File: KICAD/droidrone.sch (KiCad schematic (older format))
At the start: 48 parts, among them U4 LP2950L-3.3V, Y1 Crystal

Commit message: kicad add usb
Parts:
- removed 10k5, 10k6: 10k, lib:R-tate, symbol R
- added P?: USB_A, symbol USB_A
- U?: symbol 7805 -> 7805-RESCUE-droidrone
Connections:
- wire segments 106 -> 103
- no-connect marks 28 -> 32
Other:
- moved on the sheet: 1k1, 1k2, LED1, LED2
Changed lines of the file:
@@
 EESchema Schematic File Version 2
+LIBS:droidrone-rescue
 LIBS:power
 LIBS:device
@@
 U 1 1 580D711D
 P 4700 6700
-F 0 "RN42XV1" H 4700 7150 60  0000 C CNN
+F 0 "RN42XV1" H 4700 7050 60  0000 C CNN
 F 1 "RN42XV" H 4700 7050 60  0001 C CNN
 F 2 "lib:RN42XV" H 4700 6700 60  0001 C CNN
@@
 U 1 1 580E898B
 P 3300 6650
-F 0 "RN4020" H 3300 7250 60  0000 C CNN
+F 0 "RN4020" H 3300 7150 60  0000 C CNN
 F 1 "RN4020" H 3300 7150 60  0001 C CNN
 F 2 "lib:RN2040" H 3300 6650 60  0001 C CNN
@@
 L R 1k1
 U 1 1 580EB00D
-P 2000 6400
-F 0 "1k1" V 2080 6400 50  0000 C CNN
-F 1 "1k" V 2000 6400 50  0001 C CNN
-F 2 "lib:R-tate" V 1930 6400 50  0001 C CNN
-F 3 "" H 2000 6400 50  0000 C CNN
-	1    2000 6400
-	0    1    1    0
-$EndComp
-$Comp
-L R 1k2
-U 1 1 580EB146
-P 2000 6600
-F 0 "1k2" V 2080 6600 50  0000 C CNN
-F 1 "1k" V 2000 6600 50  0001 C CNN
-F 2 "lib:R-tate" V 1930 6600 50  0001 C CNN
-F 3 "" H 2000 6600 50  0000 C CNN
-	1    2000 6600
+P 2300 6400
+F 0 "1k1" V 2380 6400 50  0000 C CNN
+F 1 "1k" V 2300 6400 50  0001 C CNN
+F 2 "lib:R-tate" V 2230 6400 50  0001 C CNN
+F 3 "" H 2300 6400 50  0000 C CNN
+	1    2300 6400
 	0    1    1    0
 $EndComp
@@
 L LED LED1
 U 1 1 580EC3D9
-P 1650 6400
-F 0 "LED1" H 1650 6500 50  0000 C CNN
-F 1 "LED" H 1450 6500 50  0000 C CNN
-F 2 "LEDs:LED-5MM" H 1650 6400 50  0001 C CNN
-F 3 "" H 1650 6400 50  0000 C CNN
-	1    1650 6400
+P 1950 6400
+F 0 "LED1" H 1950 6500 50  0000 C CNN
+F 1 "LED" H 1750 6500 50  0000 C CNN
+F 2 "LEDs:LED-5MM" H 1950 6400 50  0001 C CNN
+F 3 "" H 1950 6400 50  0000 C CNN
+	1    1950 6400
 	1    0    0    -1
 $EndComp
@@
 L LED LED2
 U 1 1 580EC4D0
-P 1650 6600
-F 0 "LED2" H 1650 6700 50  0000 C CNN
-F 1 "LED" H 1450 6700 50  0000 C CNN
-F 2 "LEDs:LED-5MM" H 1650 6600 50  0001 C CNN
-F 3 "" H 1650 6600 50  0000 C CNN
-	1    1650 6600
+P 1950 6600
+F 0 "LED2" H 1950 6700 50  0000 C CNN
+F 1 "LED" H 1750 6700 50  0000 C CNN
+F 2 "LEDs:LED-5MM" H 1950 6600 50  0001 C CNN
+F 3 "" H 1950 6600 50  0000 C CNN
+	1    1950 6600
 	1    0    0    -1
 $EndComp
@@
 L GND #PWR049
 U 1 1 580EC7D8
-P 1450 6400
-F 0 "#PWR049" H 1450 6150 50  0001 C CNN
-F 1 "GND" H 1450 6250 50  0000 C CNN
-F 2 "" H 1450 6400 50  0000 C CNN
-F 3 "" H 1450 6400 50  0000 C CNN
-	1    1450 6400
+P 1750 6400
+F 0 "#PWR049" H 1750 6150 50  0001 C CNN
+F 1 "GND" H 1750 6250 50  0000 C CNN
+F 2 "" H 1750 6400 50  0000 C CNN
+F 3 "" H 1750 6400 50  0000 C CNN
+	1    1750 6400
 	0    1    1    0
 $EndComp
@@
 L GND #PWR050
 U 1 1 580EC8C5
-P 1450 6600
-F 0 "#PWR050" H 1450 6350 50  0001 C CNN
-F 1 "GND" H 1450 6450 50  0000 C CNN
-F 2 "" H 1450 6600 50  0000 C CNN
-F 3 "" H 1450 6600 50  0000 C CNN
-	1    1450 6600
+P 1750 6600
+F 0 "#PWR050" H 1750 6350 50  0001 C CNN
+F 1 "GND" H 1750 6450 50  0000 C CNN
+F 2 "" H 1750 6600 50  0000 C CNN
+F 3 "" H 1750 6600 50  0000 C CNN
+	1    1750 6600
 	0    1    1    0
 $EndComp
@@
 	3300 5900 3300 6000
 Connection ~ 1800 3600
-Wire Wire Line
-	10250 2250 10250 2200
 Connection ~ 3200 3600
-$Comp
-L R 10k6
-U 1 1 581115B0
-P 9150 6150
-F 0 "10k6" V 9230 6150 50  0000 C CNN
-F 1 "10k" V 9150 6150 50  0001 C CNN
-F 2 "lib:R-tate" V 9080 6150 50  0001 C CNN
-F 3 "" H 9150 6150 50  0000 C CNN
-	1    9150 6150
-	1    0    0    -1
-$EndComp
-$Comp
-L R 10k5
-U 1 1 581116D8
-P 9650 6200
-F 0 "10k5" V 9730 6200 50  0000 C CNN
-F 1 "10k" V 9650 6200 50  0001 C CNN
-F 2 "lib:R-tate" V 9580 6200 50  0001 C CNN
-F 3 "" H 9650 6200 50  0000 C CNN
-	1    9650 6200
-	1    0    0    -1
-$EndComp
 $Comp
 L +6V #PWR073
@@
 $EndComp
 Wire Wire Line
-	2150 6400 2450 6400
-Wire Wire Line
-	2150 6600 2450 6600
-Connection ~ 2200 6400
-Wire Wire Line
-	2450 6500 2250 6500
-Connection ~ 2300 6600
+	2450 6400 2450 6400
+Wire Wire Line
+	2450 6600 2450 6600
 $Comp
 L ATMEGA328P-A IC?
@@
 NoConn ~ 3400 7300
 NoConn ~ 3200 7300
-Wire Wire Line
-	2450 6900 2450 7000
 $Comp
 L GND #PWR?
@@
 $EndComp
 $Comp
-L 7805 U?
+L 7805-RESCUE-droidrone U?
 U 1 1 5888277B
 P 2200 3650
@@
 	1    0    0    -1
 $EndComp
+$Comp
+L R 1k2
+U 1 1 580EB146
+P 2300 6600
+F 0 "1k2" V 2380 6600 50  0000 C CNN
+F 1 "1k" V 2300 6600 50  0001 C CNN
+F 2 "lib:R-tate" V 2230 6600 50  0001 C CNN
+F 3 "" H 2300 6600 50  0000 C CNN
+	1    2300 6600
+	0    1    1    0
+$EndComp
+$Comp
+L +3.3V #PWR?
+U 1 1 58887043
+P 2450 6900
+F 0 "#PWR?" H 2450 6750 50  0001 C CNN
+F 1 "+3.3V" H 2450 7040 50  0000 C CNN
+F 2 "" H 2450 6900 50  0000 C CNN
+F 3 "" H 2450 6900 50  0000 C CNN
+	1    2450 6900
+	0    -1   -1   0
+$EndComp
+NoConn ~ 2450 6500
+$Comp
+L USB_A P?
+U 1 1 5889001F
+P 2700 2550
+F 0 "P?" H 2900 2350 50  0000 C CNN
+F 1 "USB_A" H 2650 2750 50  0000 C CNN
+F 2 "" V 2650 2450 50  0000 C CNN
+F 3 "" V 2650 2450 50  0000 C CNN
+	1    2700 2550
+	1    0    0    -1
+$EndComp
+NoConn ~ 2600 2850
+NoConn ~ 2700 2850
+$Comp
+L +5V #PWR?
+U 1 1 5889070E
+P 2500 2850
+F 0 "#PWR?" H 2500 2700 50  0001 C CNN
+F 1 "+5V" H 2500 2990 50  0000 C CNN
+F 2 "" H 2500 2850 50  0000 C CNN
+F 3 "" H 2500 2850 50  0000 C CNN
+	1    2500 2850
+	-1   0    0    1
+$EndComp
+$Comp
+L GND #PWR?
+U 1 1 58890B52
+P 2800 2850
+F 0 "#PWR?" H 2800 2600 50  0001 C CNN
+F 1 "GND" H 2800 2700 50  0000 C CNN
+F 2 "" H 2800 2850 50  0000 C CNN
+F 3 "" H 2800 2850 50  0000 C CNN
+	1    2800 2850
+	1    0    0    -1
+$EndComp
+NoConn ~ 3000 2450
 $EndSCHEMATC

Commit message: kicad chg1.
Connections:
- wire segments 103 -> 104
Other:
- moved on the sheet: P?
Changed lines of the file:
@@
 	6200 3800 6200 3900
 Wire Wire Line
-	6200 3900 6750 3900
-Wire Wire Line
-	6750 3900 6750 3550
+	6750 3900 6200 3900
+Wire Wire Line
+	6750 3600 6750 3900
 Connection ~ 6750 3700
 Wire Wire Line
 	6750 3450 6450 3450
 Wire Wire Line
-	6450 3350 6450 3700
+	6450 3300 6450 3700
 Connection ~ 6450 3700
 Wire Wire Line
-	7050 3450 7200 3450
-Wire Wire Line
-	7050 3450 7050 3700
+	7050 3400 7050 3700
 $Comp
 L GND #PWR?
@@
 L CONN_01X03 P?
 U 1 1 587C7767
-P 7400 3450
-F 0 "P?" H 7400 3650 50  0000 C CNN
-F 1 "CONN_01X03" V 7500 3450 50  0000 C CNN
-F 2 "" H 7400 3450 50  0000 C CNN
-F 3 "" H 7400 3450 50  0000 C CNN
-	1    7400 3450
-	1    0    0    -1
-$EndComp
-Wire Wire Line
-	6450 3350 7200 3350
+P 7400 3400
+F 0 "P?" H 7400 3600 50  0000 C CNN
+F 1 "CONN_01X03" V 7500 3400 50  0000 C CNN
+F 2 "" H 7400 3400 50  0000 C CNN
+F 3 "" H 7400 3400 50  0000 C CNN
+	1    7400 3400
+	1    0    0    -1
+$EndComp
+Wire Wire Line
+	6450 3300 7200 3300
 Connection ~ 6450 3450
 Connection ~ 7050 3450
 Wire Wire Line
-	6750 3550 7200 3550
+	6750 3600 7200 3600
 NoConn ~ 3500 7300
 NoConn ~ 3400 7300
@@
 $EndComp
 NoConn ~ 3000 2450
+Wire Wire Line
+	7200 3600 7200 3500
+Wire Wire Line
+	7050 3400 7200 3400
 $EndSCHEMATC

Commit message: kicad add usb
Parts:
- removed IC?: ATMEGA328P-A, TQFP32, symbol ATMEGA328P-A
- removed P?: CONN_01X03, symbol CONN_01X03
- added 0.1uF2: 0.1uF, Capacitors_ThroughHole:C_Rect_L4_W2.5_P2.5, symbol C
- added 10k4: 10k, lib:R-tate, symbol R
- added D17: CONN_01X03, Pin_Headers:Pin_Header_Straight_1x03, symbol CONN_01X03
- added IC1: ATMEGA328PB, lib:LQFP-32_7x7mm_Pitch0.8mm, symbol ATMEGA328PB
- added P4, P7: CONN_01X02, Pin_Headers:Pin_Header_Straight_1x02_Pitch2.54mm, symbol CONN_01X02
- added P5: CONN_01X04, Pin_Headers:Pin_Header_Straight_1x04_Pitch2.00mm, symbol CONN_01X04
- P2, P3: renamed from P?; footprint (none) -> Pin_Headers:Pin_Header_Straight_1x06_Pitch2.54mm
- P6: renamed from P?; footprint (none) -> Pin_Headers:Pin_Header_Straight_1x04_Pitch2.00mm
- Y1: footprint Crystals:Crystal_HC52-U_Vertical -> Crystals:Crystal_HC49-U-3pin_Vertical
- gave numbers to parts that had none: 2
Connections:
- wire segments 104 -> 120
- no-connect marks 32 -> 29
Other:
- moved on the sheet: 0.1uF5, 0.1uF6, 10k1, 10k2, 10k3, 1k4, 1k5, D10, D12, D13, D14, D15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

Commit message: foot print update
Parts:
- 0.1uF1, 0.1uF2, 0.1uF4, 0.1uF5, 0.1uF6, 22pF1, 22pF2: footprint Capacitors_ThroughHole:C_Rect_L4_W2.5_P2.5 -> Capacitors_ThroughHole:C_Rect_L4.0mm_W2.5mm_P2.50mm
- 100uF10V1, 47uF10V1: footprint Capacitors_ThroughHole:C_Radial_D5_L6_P2.5 -> Capacitors_ThroughHole:CP_Radial_D8.0mm_P2.50mm
- 10k1, 10k2, 10k3, 10k4, 1k1, 1k2, 1k3, 1k4, 1k5, 2.2k1, 3.3k1: footprint lib:R-tate -> Resistors_ThroughHole:R_Axial_DIN0204_L3.6mm_D1.6mm_P2.54mm_Vertical
- D10, D12, D13, D14, D15, D16, D17, D2, D4, D7, D8, D9: footprint Pin_Headers:Pin_Header_Straight_1x03 -> Pin_Headers:Pin_Header_Straight_1x03_Pitch2.54mm
- LED1, LED2, LED3, LED4: footprint LEDs:LED-5MM -> LEDs:LED_D5.0mm
- No-BEC1: footprint Pin_Headers:Pin_Header_Straight_1x02 -> Pin_Headers:Pin_Header_Straight_1x02_Pitch2.54mm
- P1: footprint (none) -> Connect:USB_A
- P6: footprint Pin_Headers:Pin_Header_Straight_1x04_Pitch2.00mm -> Pin_Headers:Pin_Header_Straight_1x06_Pitch2.54mm
- U1: footprint (none) -> TO_SOT_Packages_THT:TO-220_Neutral123_Vertical_LargePads

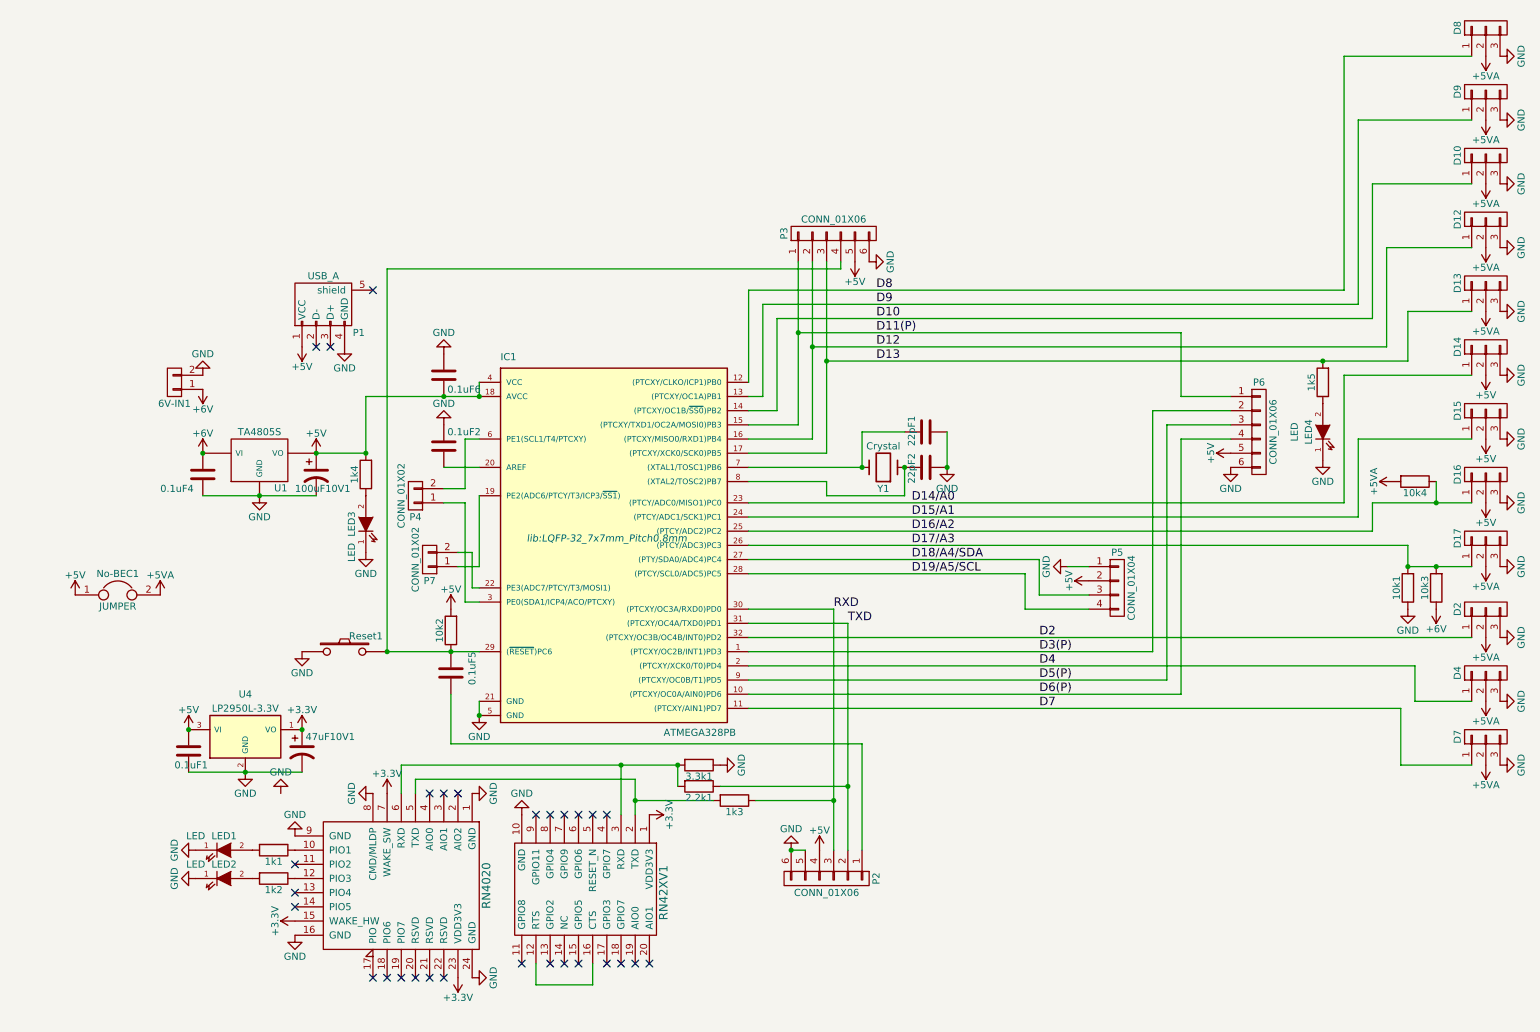
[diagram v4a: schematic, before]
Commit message: add sub pcb
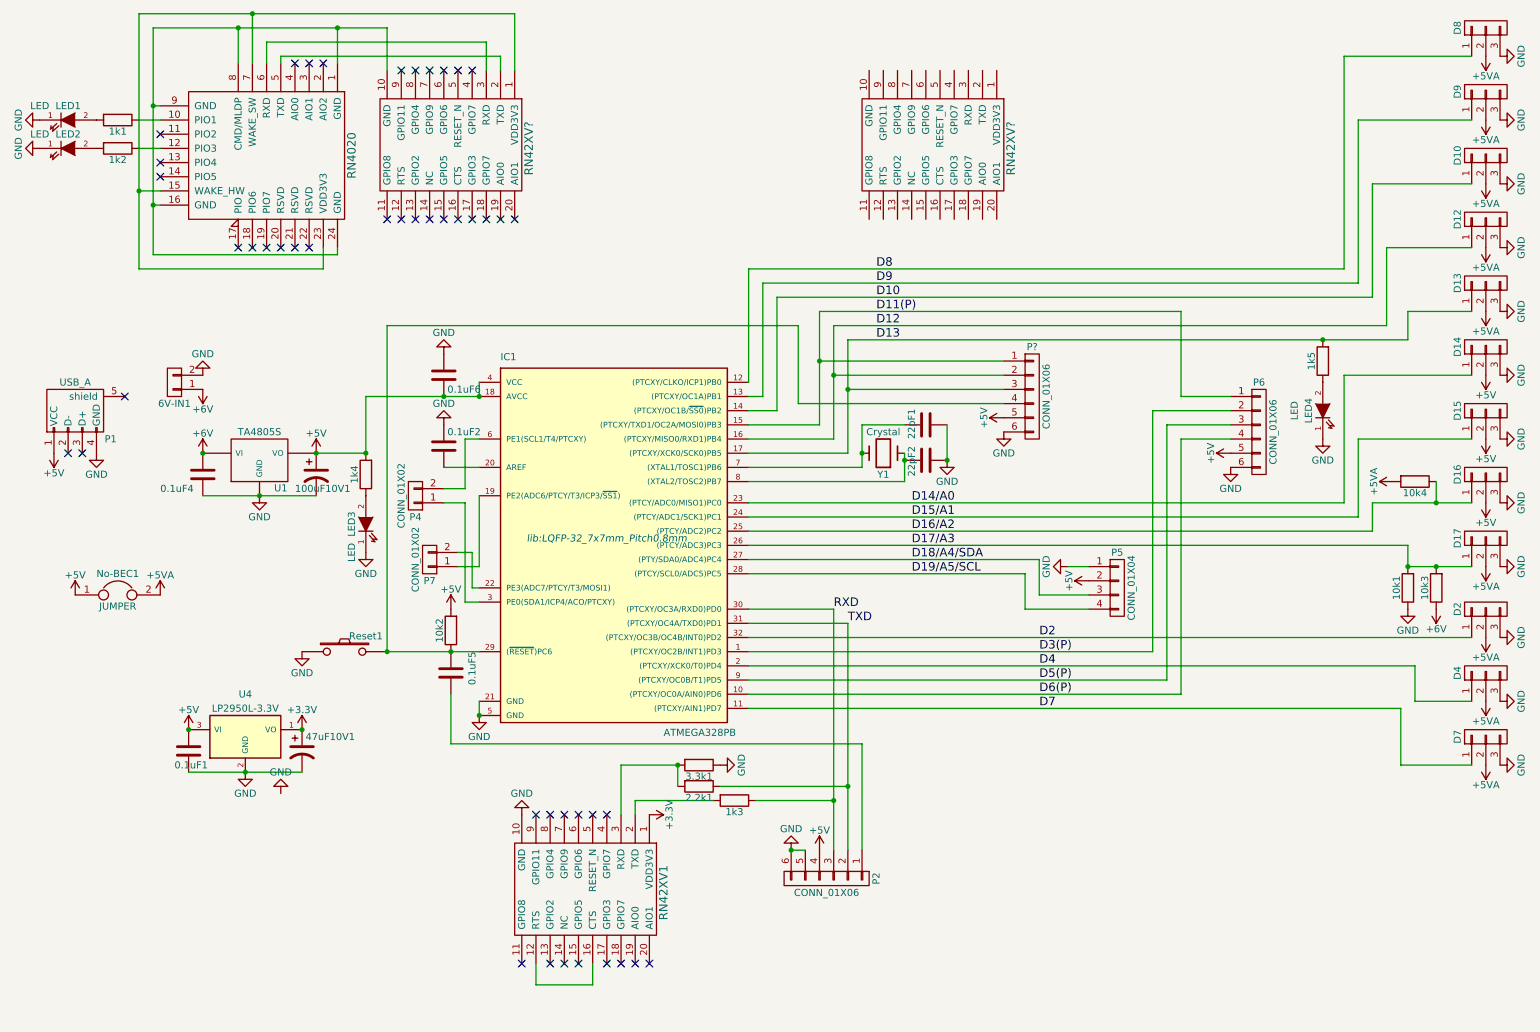
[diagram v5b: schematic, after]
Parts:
- removed P3: CONN_01X06, Pin_Headers:Pin_Header_Straight_1x06_Pitch2.54mm, symbol CONN_01X06
- added P?: CONN_01X06, Pin_Headers:Pin_Header_Straight_1x06_Pitch2.54mm, symbol CONN_01X06
- added RN42XV? (x2): RN42XV, lib:RN42XV, symbol RN42XV
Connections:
- net +3V3: no longer RN4020.15 (WAKE_HW), RN4020.23 (VDD3V3), RN4020.7 (WAKE_SW)
- net +5V: now also P?.5 (P5)
- net D11(P): now also P?.1 (P1)
- net D12: now also P?.2 (P2)
- net D13: now also P?.3 (P3)
- net GND: now also P?.6 (P6); no longer RN4020.1 (GND), RN4020.16 (GND), RN4020.24 (GND), RN4020.8 (CMD/MLDP), RN4020.9 (GND)
- net at 0.1uF5.2, 10k2.1, IC1.29 ((~RESET~)PC6)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: now also P?.4 (P4)
- net at 1k3.2, RN42XV1.2 (TXD): no longer RN4020.5 (TXD)
- net at 2.2k1.2, 3.3k1.2, RN42XV1.3 (RXD): no longer RN4020.6 (RXD)
- new net: RN4020.1 (GND), RN4020.16 (GND), RN4020.24 (GND), RN4020.8 (CMD/MLDP), RN4020.9 (GND), RN42XV?.10 (GND)
- new net: RN4020.15 (WAKE_HW), RN4020.23 (VDD3V3), RN4020.7 (WAKE_SW), RN42XV?.1 (VDD3V3)
- new net: RN4020.5 (TXD), RN42XV?.2 (TXD)
- new net: RN4020.6 (RXD), RN42XV?.3 (RXD)
- no-connect marks 29 -> 45
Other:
- moved on the sheet: 1k1, 1k2, 1k5, 22pF1, 22pF2, LED1, LED2, LED4, P1, RN4020, Y1

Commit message: same chg.
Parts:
- removed RN42XV?: RN42XV, lib:RN42XV, symbol RN42XV
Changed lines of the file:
@@
-	0    1    1    0
-$EndComp
-$Comp
-L RN42XV RN42XV?
-U 1 1 589D8622
-P 7150 1450
-F 0 "RN42XV?" H 7150 1800 60  0000 C CNN
-F 1 "RN42XV" H 7150 1800 60  0001 C CNN
-F 2 "lib:RN42XV" H 7150 1450 60  0001 C CNN
-F 3 "" H 7150 1450 60  0000 C CNN
-	1    7150 1450
 	0    1    1    0
 $EndComp

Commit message: chg sch
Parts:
- removed P4, P7: CONN_01X02, Pin_Headers:Pin_Header_Straight_1x02_Pitch2.54mm, symbol CONN_01X02
- added 2.2k2, 2.2k3, 2.2k4, 2.2k5: 2.2k, Resistors_ThroughHole:R_Axial_DIN0204_L3.6mm_D1.6mm_P2.54mm_Vertical, symbol R
- added GrI2C-S1, GrI2C1, GroveAna1: CONN_01X04, Pin_Headers:Pin_Header_Straight_1x04_Pitch2.00mm, symbol CONN_01X04
- gave numbers to parts that had none: 2
- renumbered LED1 to Conn1, P5 to GrI2C2, LED4 to L-D13, P6 to PWM1, LED3 to Pow1, P2 to UART1, LED2 to WakeUp1
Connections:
- net +5V: now also 10k2.1, 2.2k2.1, 2.2k3.2, 2.2k4.1, 2.2k5.1, GrI2C-S1.2 (P2), GrI2C1.2 (P2), GroveAna1.2 (P2); no longer 10k2.2
- net D18/A4/SDA: now also 2.2k4.2, GrI2C1.3 (P3)
- net D19/A5/SCL: now also 2.2k5.2, GrI2C1.4 (P4)
- net GND: now also GrI2C-S1.1 (P1), GrI2C1.1 (P1), GroveAna1.1 (P1)
- net at 0.1uF5.2, IC1.29 ((~RESET~)PC6), ISP1.4 (P4)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: now also 10k2.2; no longer 10k2.1
- net at IC1.19 (PE2(ADC6/PTCY/T3/ICP3/~SS1)): now also GroveAna1.4 (P4)
- net at IC1.22 (PE3(ADC7/PTCY/T3/MOSI1)): now also GroveAna1.3 (P3)
- net at IC1.3 (PE0(SDA1/ICP4/ACO/PTCXY)): now also 2.2k3.1, GrI2C-S1.3 (P3)
- net at IC1.6 (PE1(SCL1/T4/PTCXY)): now also 2.2k2.2, GrI2C-S1.4 (P4)
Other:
- moved on the sheet: 0.1uF1, 0.1uF2, 0.1uF4, 100uF10V1, 10k2, 1k4, 22pF1, 22pF2, 47uF10V1, 6V-IN1, No-BEC1, P1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
